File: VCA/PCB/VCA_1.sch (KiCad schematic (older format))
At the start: 64 parts

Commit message: work on scematics
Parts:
- removed J? (x2): Audio-Jack-2, symbol Audio-Jack-2
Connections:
- net labels removed: Earth
- wire segments 176 -> 65

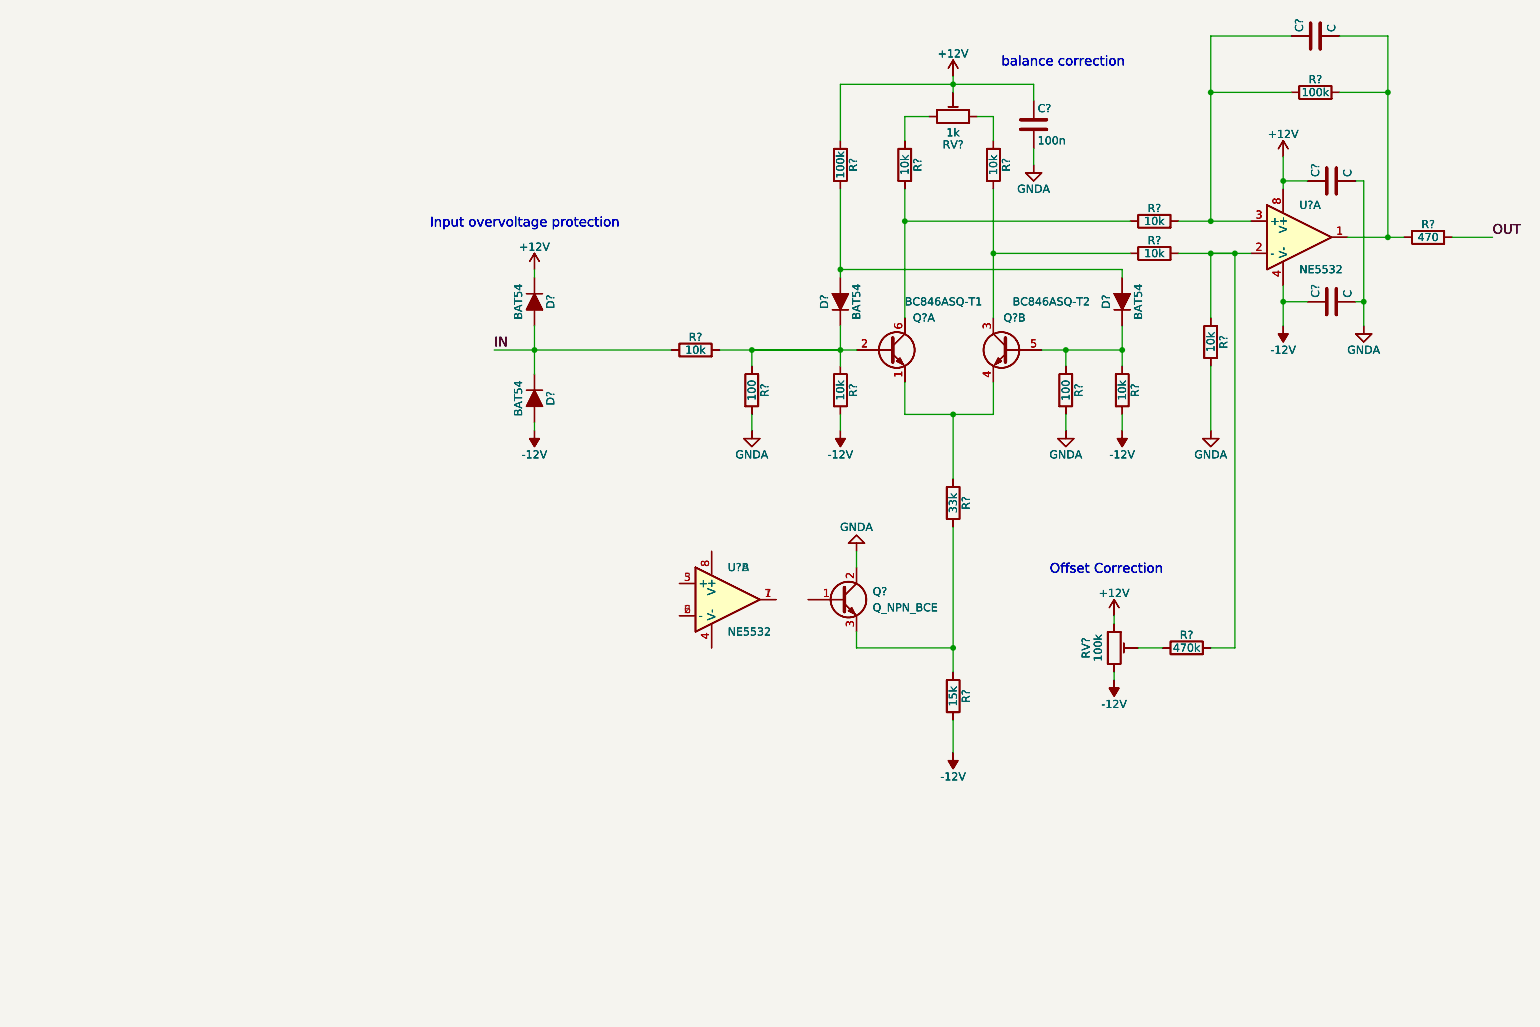
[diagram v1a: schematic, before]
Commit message: scematic design of vca
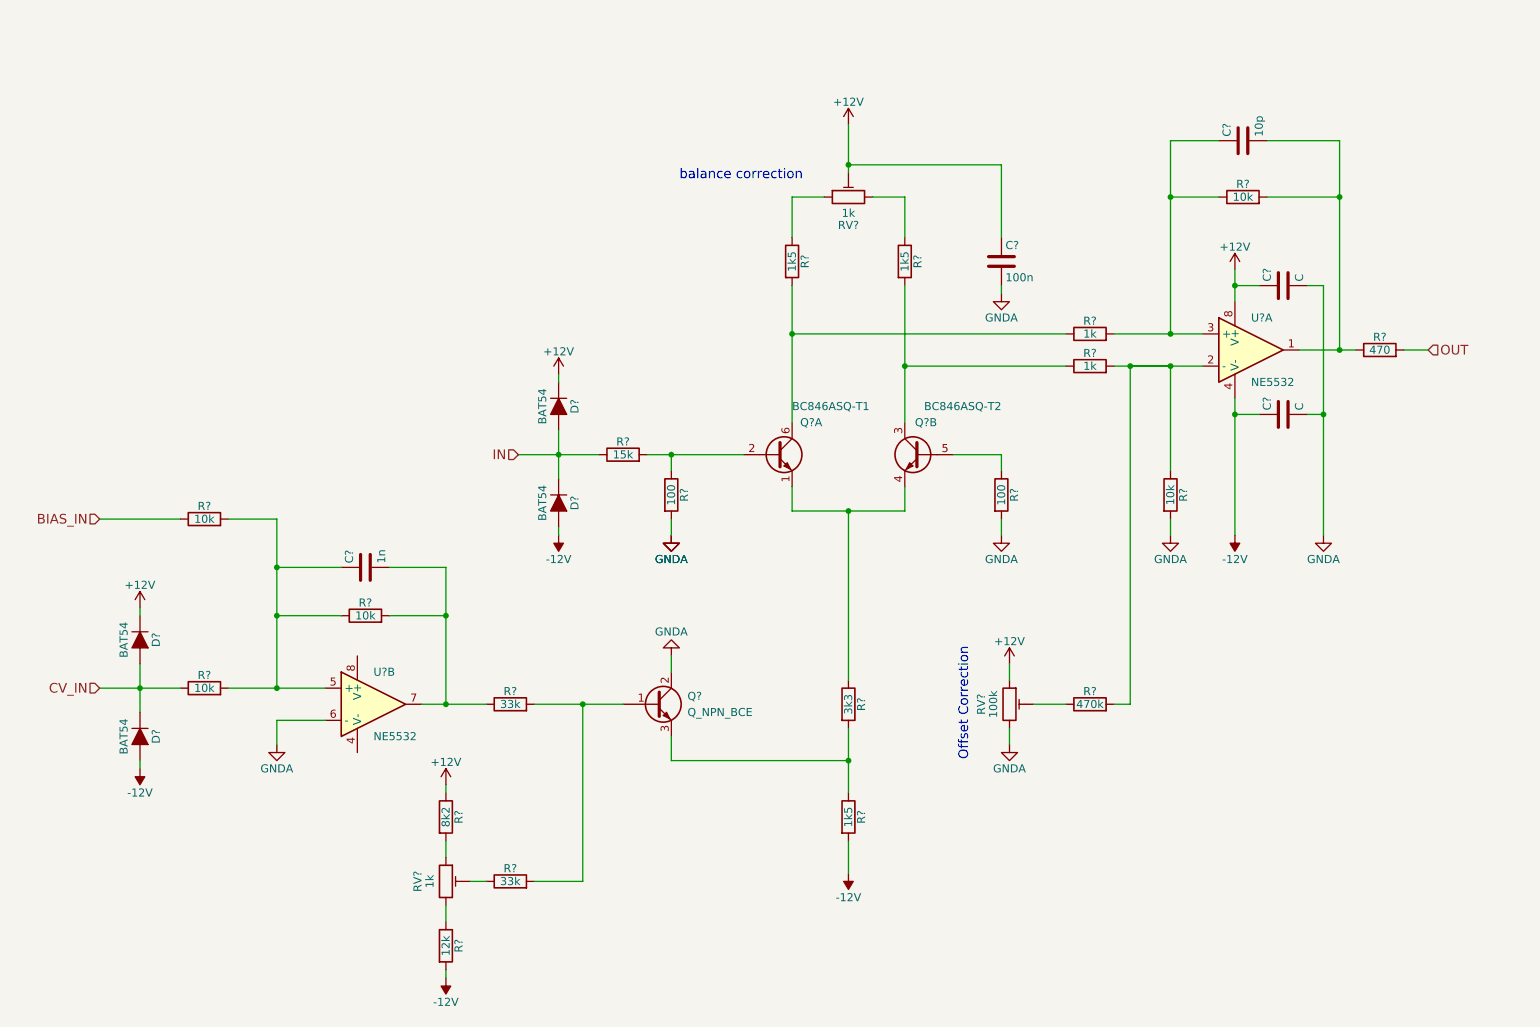
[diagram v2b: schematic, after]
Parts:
- removed C? (x3): C, symbol C
- removed C?: 100n, symbol C
- removed D? (x6): BAT54, Diodes_SMD:D_SOT-23_ANK, symbol D_ALT
- removed Q?: BC846ASQ-T1, TO_SOT_Packages_SMD:SOT-363_SC-70-6_Handsoldering, symbol Q_DUAL_NPN_NPN_E1B1C2E2B2C1
- removed Q?: BC846ASQ-T2, TO_SOT_Packages_SMD:SOT-363_SC-70-6_Handsoldering, symbol Q_DUAL_NPN_NPN_E1B1C2E2B2C1
- removed Q?: Q_NPN_BCE, symbol Q_NPN_BCE
- removed R? (x10): 10k, Resistors_SMD:R_0603_HandSoldering, symbol R
- removed R? (x2): 100, Resistors_SMD:R_0603_HandSoldering, symbol R
- removed R? (x3): 100k, Resistors_SMD:R_0603_HandSoldering, symbol R
- removed R?: 33k, Resistors_SMD:R_0603_HandSoldering, symbol R
- removed R?: 15k, Resistors_SMD:R_0603_HandSoldering, symbol R
- removed R?: 470k, Resistors_SMD:R_0603_HandSoldering, symbol R
- removed R?: 470, Resistors_SMD:R_0603_HandSoldering, symbol R
- removed RV?: 1k, Potentiometers:Potentiometer_Trimmer_Bourns_3299Y, symbol POT_TRIM
- removed RV?: 100k, Potentiometers:Potentiometer_Trimmer_Bourns_3299Y, symbol POT_TRIM
- removed U?: NE5532, Housings_SOIC:SO-8_5.3x6.2mm_Pitch1.27mm, symbol NE5532
- removed U?: NE5532, symbol NE5532
- added C?: 1n, symbol C
- added D? (x2): BAT54, Diodes_SMD:D_SOT-23_ANK, symbol D_ALT
- added R? (x3): 10k, Resistors_SMD:R_0603_HandSoldering, symbol R
- added R?: 8k2, Resistors_SMD:R_0603_HandSoldering, symbol R
- added R?: 12k, Resistors_SMD:R_0603_HandSoldering, symbol R
- added R? (x2): 33k, Resistors_SMD:R_0603_HandSoldering, symbol R
- added RV?: 1k, Potentiometers:Potentiometer_Trimmer_Bourns_3299Y, symbol POT_TRIM
- C?: value C -> 10p
- R?: value 10k -> 15k
- R?: value 100k -> 10k
- R? (x2): value 10k -> 1k5
- R? (x2): value 10k -> 1k
- R?: value 33k -> 3k3
- R?: value 15k -> 1k5
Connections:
- net +12V: now also D?.1 (K), R?.1
- net -12V: now also D?.2 (A), R?.2; no longer RV?.3
- net GNDA: now also RV?.3, U?.6 (-)
- net IN: now also D?.1 (K), D?.2 (A); no longer D?.1 (K), D?.2 (A)
- net at Q?.1 (B): now also R?.2, R?.2
- net at U?.5 (+): now also C?.1, R?.1, R?.2, R?.2
- net at U?.7: now also C?.2, R?.1, R?.2
- new net: R?.2, RV?.1
- new net: R?.1, RV?.3
- new net: R?.1, RV?.2
- new net BIAS_IN: R?.1
- new net CV_IN: D?.1 (K), D?.2 (A), R?.1
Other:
- note removed: "Input overvoltage protection"
- moved on the sheet: C?, D?, Q?, Q?A, Q?B, R?, RV?, U?A, U?B
